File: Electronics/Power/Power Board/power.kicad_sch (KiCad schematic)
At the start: 58 parts, among them IC3 INA219AIDR, IC6 TPS54295PWPR, IC7 MP28167GQ-A-Z, J1 XT60PW-M, J3 XT60PW-F, SW1 SW_SPDT

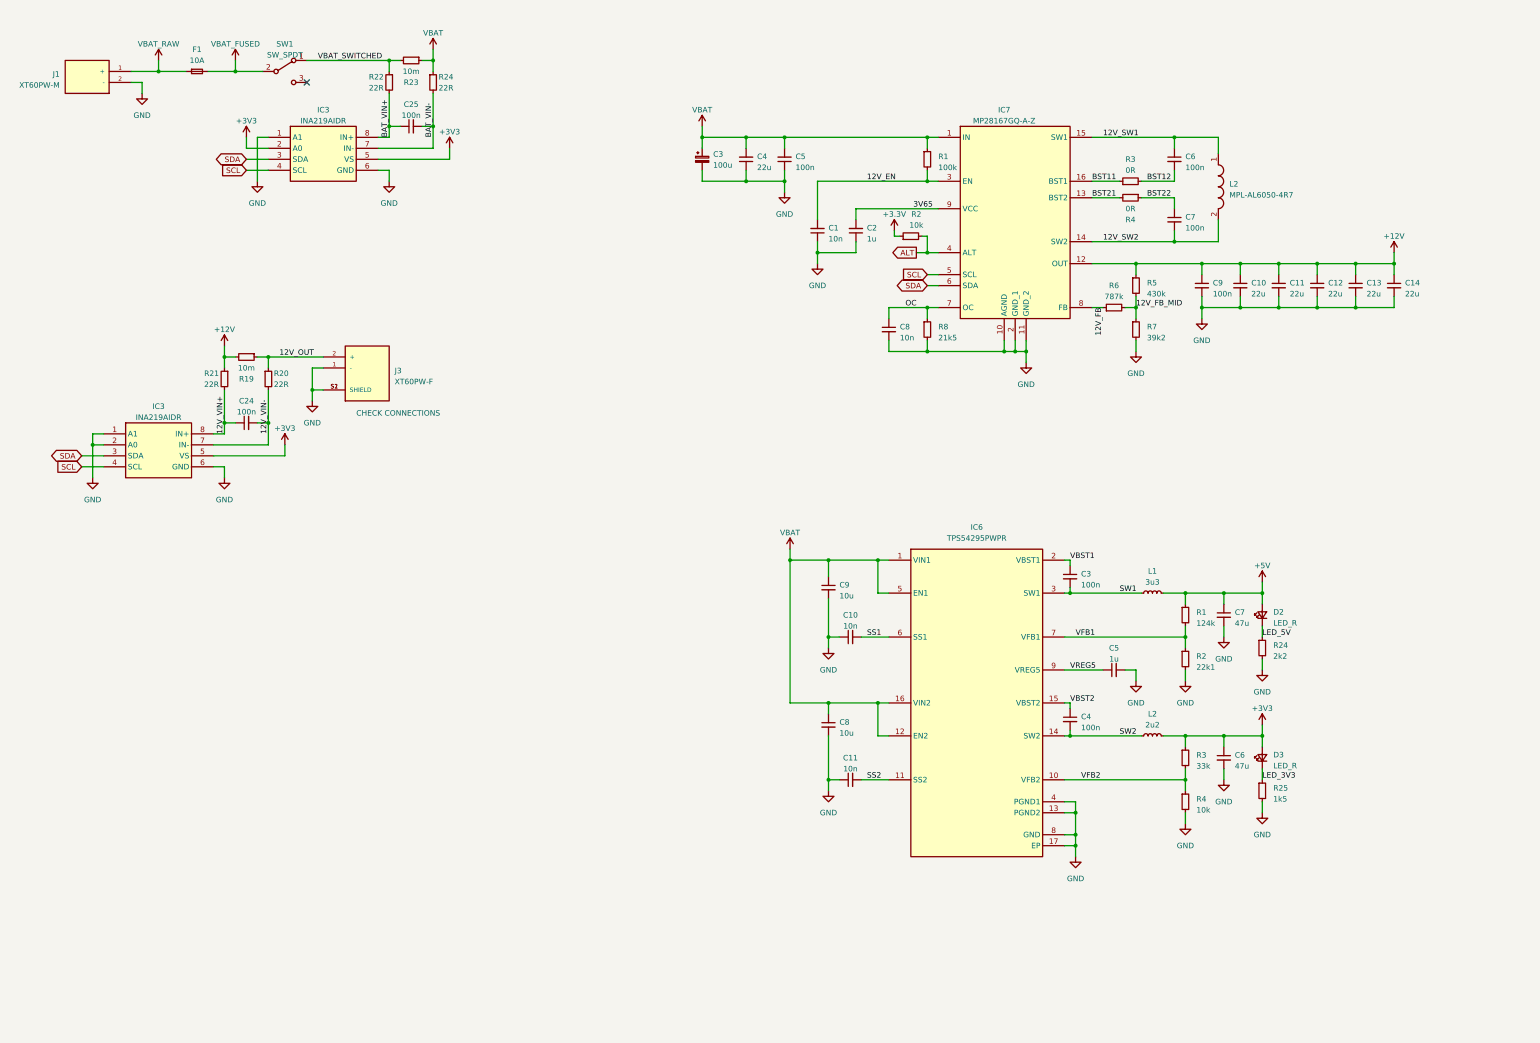
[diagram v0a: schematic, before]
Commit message: Motor driver + power board progress
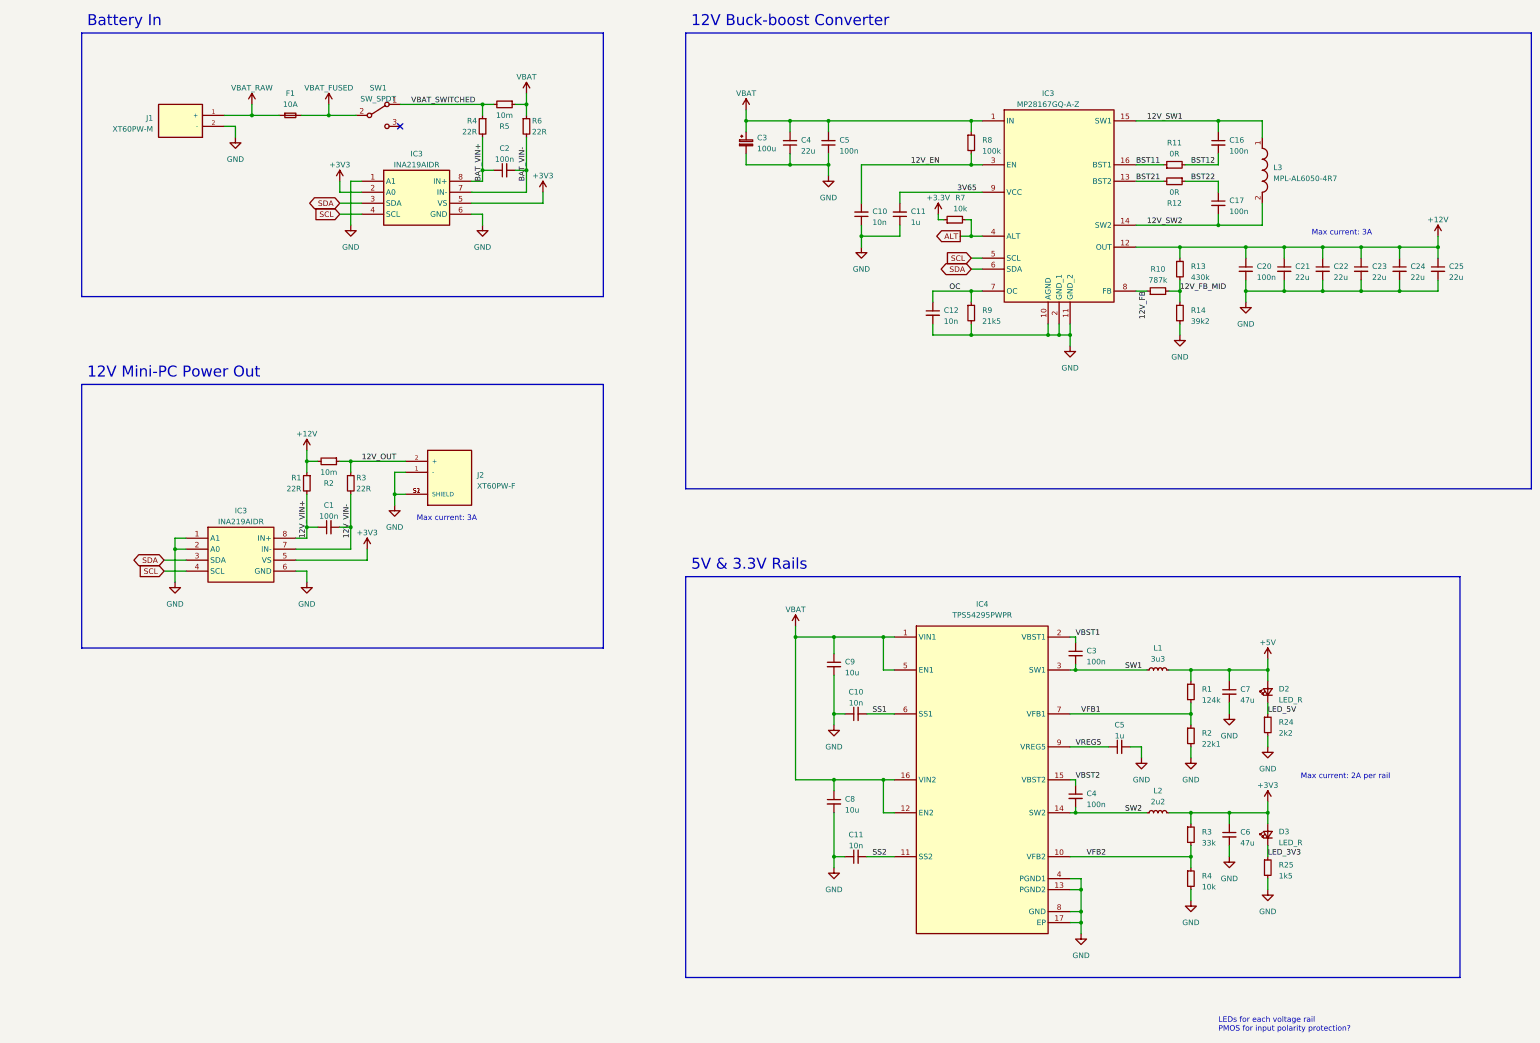
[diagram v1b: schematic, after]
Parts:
- SW1: footprint (none) -> MSL Footprints:Toggle_switch
- renumbered C24 to C1, C1 to C10, C2 to C11, C8 to C12, C6 to C16, C7 to C17, C25 to C2, C9 to C20, C10 to C21, C11 to C22, C12 to C23, C13 to C24, C14 to C25, IC7 to IC3, IC6 to IC4, J3 to J2, L2 to L3, R21 to R1, R6 to R10, R3 to R11, R4 to R12, R5 to R13, R7 to R14, R19 to R2, R20 to R3, R22 to R4, R23 to R5, R24 to R6, R2 to R7, R1 to R8, R8 to R9
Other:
- note added: "12V Buck-boost Converter"
- note added: "12V Mini-PC Power Out"
- note added: "5V & 3.3V Rails"
- note added: "Battery In"
- note added: "LEDs for each voltage rail PMOS for input polarity protection?"
- note added: "Max current: 2A per rail"
- note added: "Max current: 3A"
- note removed: "CHECK CONNECTIONS"
- moved on the sheet: C1, C10, C11, C12, C16, C17, C2, C20, C21, C22, C23, C24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

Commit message: PCB Schematic progress
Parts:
- removed C4: 22u, Capacitor_SMD:C_0402_1005Metric, symbol Device:C_Small
- added C42: 22u, Capacitor_SMD:C_0805_2012Metric, symbol Device:C_Small
- added J10, J11 (x2), J9: Conn_01x02_Pin, Connector_PinHeader_2.54mm:PinHeader_1x02_P2.54mm_Vertical, symbol Connector:Conn_01x02_Pin
- added J2 (x6): Screw_Terminal_01x02, TerminalBlock:TerminalBlock_bornier-2_P5.08mm, symbol Connector:Screw_Terminal_01x02
- C21, C22, C23, C24, C25: footprint Capacitor_SMD:C_0402_1005Metric -> Capacitor_SMD:C_0805_2012Metric
- C3: footprint (none) -> Capacitor_SMD:CP_Elec_6.3x7.7
- C8, C9: footprint Capacitor_SMD:C_0402_1005Metric -> Capacitor_SMD:C_0603_1608Metric
- D2, D3: value LED_R -> Green
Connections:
- net +5V: now also J10.1 (Pin_1), J11.1 (Pin_1), J11.1 (Pin_1), J9.1 (Pin_1)
- net GND: now also C42.2, J10.2 (Pin_2), J11.2 (Pin_2), J11.2 (Pin_2), J2.2 (Pin_2), J2.2 (Pin_2), J2.2 (Pin_2), J2.2 (Pin_2), J2.2 (Pin_2), J2.2 (Pin_2), J9.2 (Pin_2)
- net VBAT: now also C42.1, J2.1 (Pin_1), J2.1 (Pin_1), J2.1 (Pin_1), J2.1 (Pin_1), J2.1 (Pin_1), J2.1 (Pin_1)
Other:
- note added: "5V Fan Headers"
- note added: "VOUT Connectors"
- note removed: "LEDs for each voltage rail PMOS for input polarity protection?"
- moved on the sheet: C1, C10, C11, C12, C16, C17, C2, C20, C21, C3, C4, C5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

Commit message: PCB Schematics finished
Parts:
- renumbered C1 to C201, C2 to C202, C3 to C203, C42 to C204, C5 to C205, C10 to C210, C11 to C211, C12 to C212, C16 to C216, C17 to C217, C20 to C220, C21 to C221, C22 to C222, C23 to C223, C24 to C224, C25 to C225, IC3 to IC203, IC4 to IC204, J1 to J202, J2 to J209, L3 to L203, R1 to R201, R2 to R202, R3 to R203, R4 to R204, R5 to R205, R6 to R206, R7 to R207, R8 to R208, R9 to R209, R10 to R210, R11 to R211, R12 to R212, R13 to R213, R14 to R214, SW1 to SW201

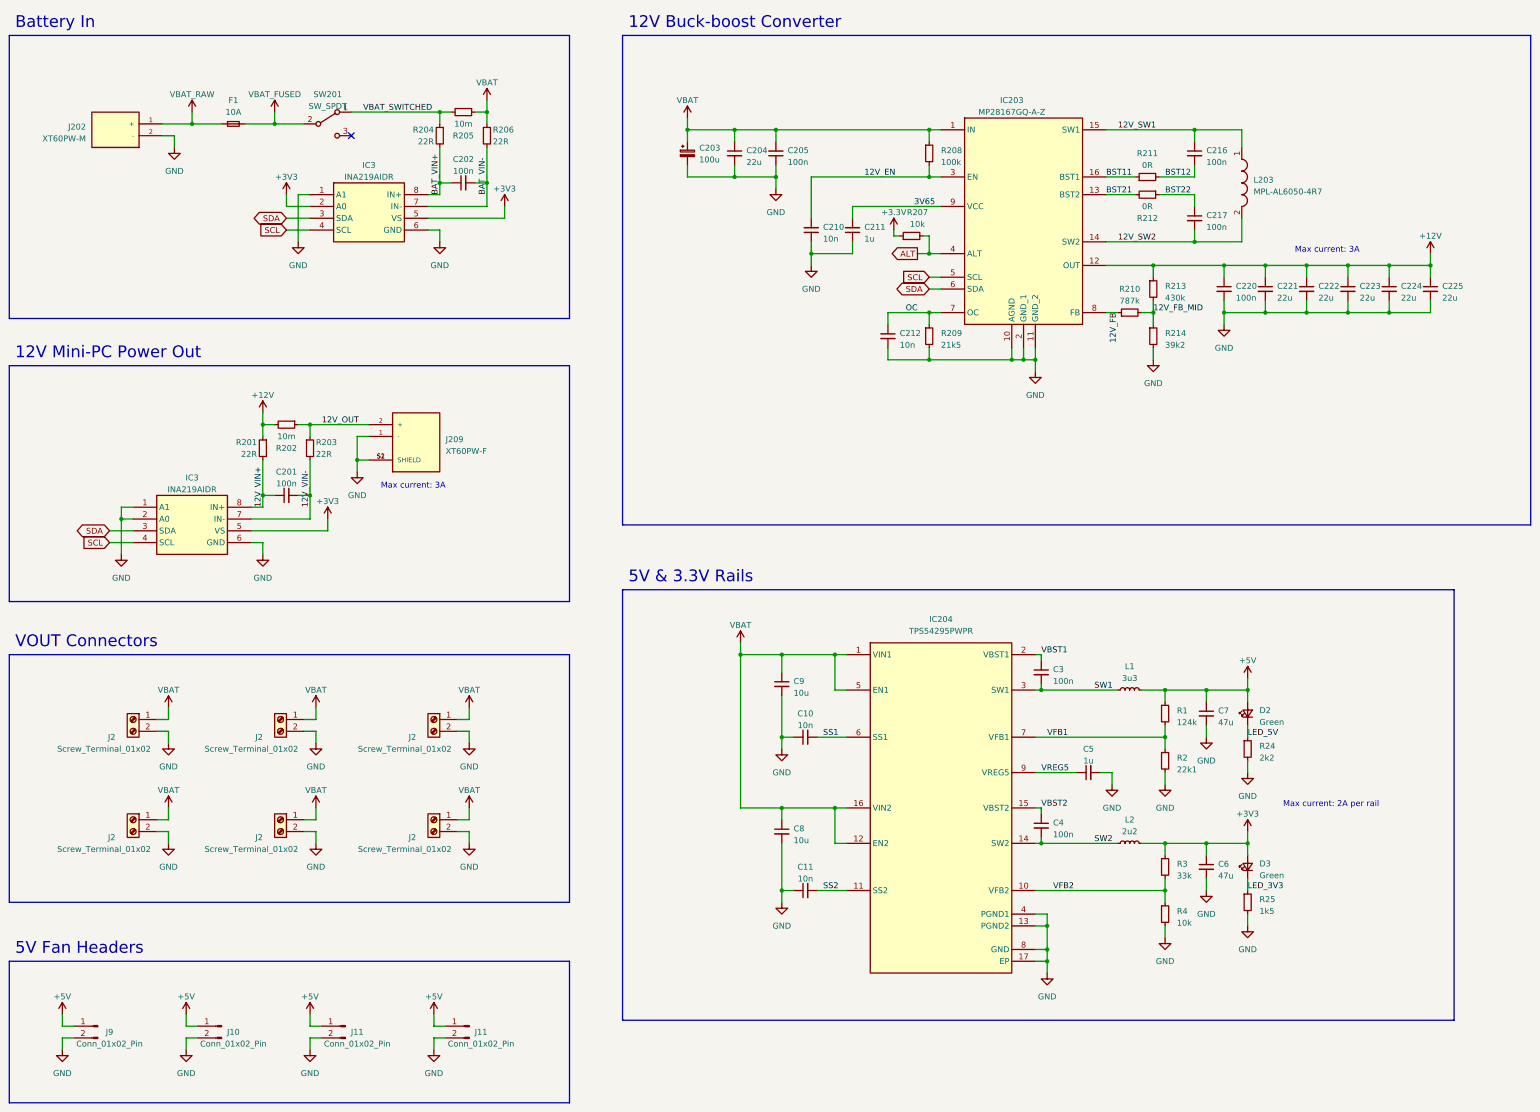
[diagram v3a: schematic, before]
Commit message: Schematic updates
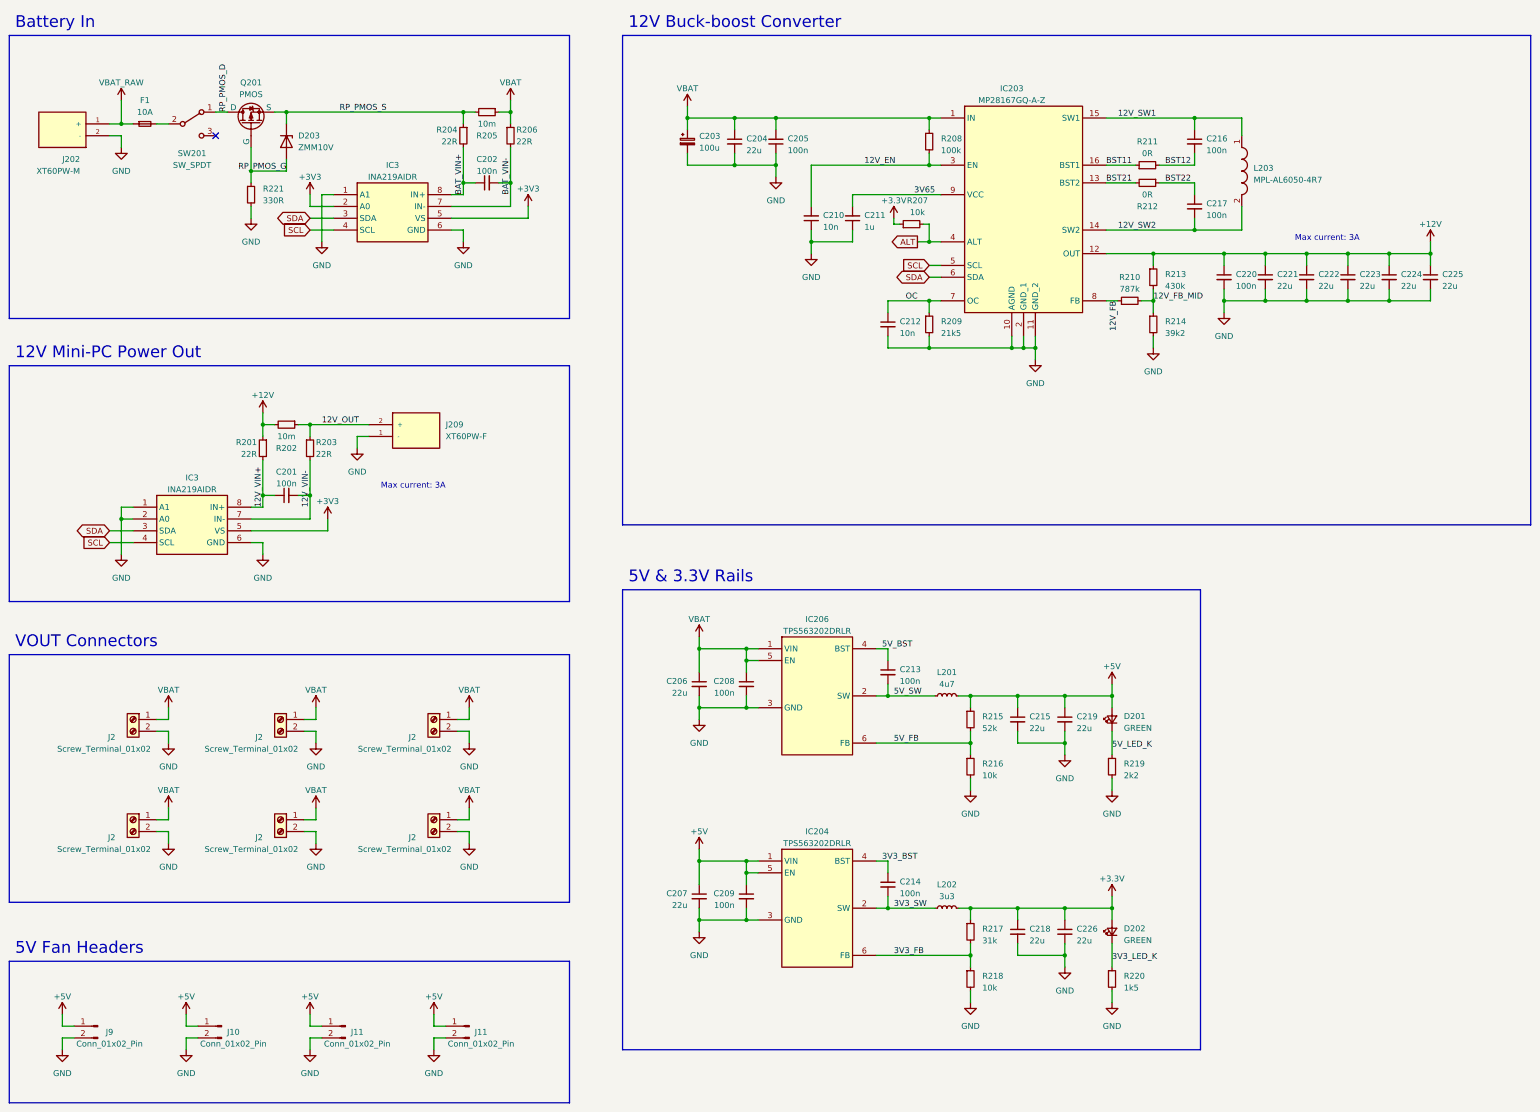
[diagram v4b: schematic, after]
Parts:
- removed C10, C11: 10n, Capacitor_SMD:C_0402_1005Metric, symbol Device:C_Small
- removed C3, C4: 100n, Capacitor_SMD:C_0402_1005Metric, symbol Device:C_Small
- removed C5: 1u, Capacitor_SMD:C_0402_1005Metric, symbol Device:C_Small
- removed C6, C7: 47u, Capacitor_SMD:C_0805_2012Metric, symbol Device:C_Small
- removed C8, C9: 10u, Capacitor_SMD:C_0603_1608Metric, symbol Device:C_Small
- removed D2, D3: Green, LED_SMD:LED_0603_1608Metric, symbol Device:LED_Small
- removed IC204: TPS54295PWPR, SOP65P640X120-17N, symbol TPS54295PWPR:TPS54295PWPR
- removed L1: 3u3, MSL Footprints:29332C, symbol Device:L_Small
- removed L2: 2u2, MSL Footprints:29222C, symbol Device:L_Small
- removed R1: 124k, Resistor_SMD:R_0402_1005Metric, symbol Device:R_Small
- removed R2: 22k1, Resistor_SMD:R_0402_1005Metric, symbol Device:R_Small
- removed R24: 2k2, Resistor_SMD:R_0402_1005Metric, symbol Device:R_Small
- removed R25: 1k5, Resistor_SMD:R_0402_1005Metric, symbol Device:R_Small
- removed R3: 33k, Resistor_SMD:R_0402_1005Metric, symbol Device:R_Small
- removed R4: 10k, Resistor_SMD:R_0402_1005Metric, symbol Device:R_Small
- added C206, C207, C215, C218, C219, C226: 22u, Capacitor_SMD:C_0603_1608Metric, symbol Device:C_Small
- added C208, C209, C213, C214: 100n, Capacitor_SMD:C_0402_1005Metric, symbol Device:C_Small
- added D201, D202: GREEN, LED_SMD:LED_0603_1608Metric, symbol Device:LED_Small
- added D203: ZMM10V, Diode_SMD:D_MiniMELF, symbol Diode:ZMMxx
- added IC204, IC206: TPS563202DRLR, MSL Footprints:SOTFL50P160X60-6N, symbol TPS563202DRLR:TPS563202DRLR
- added L201: 4u7, Inductor_SMD:L_Chilisin_BMRA00040420, symbol Device:L_Small
- added L202: 3u3, Inductor_SMD:L_Chilisin_BMRA00040420, symbol Device:L_Small
- added Q201: PMOS, symbol Simulation_SPICE:PMOS
- added R215: 52k, Resistor_SMD:R_0402_1005Metric, symbol Device:R_Small
- added R216, R218: 10k, Resistor_SMD:R_0402_1005Metric, symbol Device:R_Small
- added R217: 31k, Resistor_SMD:R_0402_1005Metric, symbol Device:R_Small
- added R219: 2k2, Resistor_SMD:R_0402_1005Metric, symbol Device:R_Small
- added R220: 1k5, Resistor_SMD:R_0402_1005Metric, symbol Device:R_Small
- added R221: 330R, Resistor_SMD:R_0402_1005Metric, symbol Device:R_Small
- IC203: footprint MSL Footprints:MP28167GQAZ -> MP28167GQAZ
- J202: footprint MSL Footprints:AMASS_XT60PW-M -> Connector_AMASS:AMASS_XT60PW-M_1x02_P7.20mm_Horizontal
- J209: footprint AMASS_XT60PW-F -> Connector_AMASS:AMASS_XT60PW-F_1x02_P7.20mm_Horizontal
- L203: footprint MSL Footprints:MPLAL60504R7 -> MPLAL60504R7
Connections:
- net +3.3V: now also C218.1, C226.1, D202.2 (A), L202.2, R217.1
- net +5V: now also C207.1, C209.1, C215.1, C219.1, D201.2 (A), IC204.1 (VIN), IC204.5 (EN), L201.2, R215.1
- net GND: now also C206.2, C207.2, C208.2, C209.2, C215.2, C218.2, C219.2, C226.2, IC204.3 (GND), IC206.3 (GND), R216.2, R218.2, R219.2, R220.2, R221.2; no longer J209.S1 (SHIELD), J209.S2 (SHIELD)
- net VBAT: now also C206.1, C208.1, IC206.1 (VIN), IC206.5 (EN)
- net VBAT_FUSED: no longer names the net of F1.2, SW201.2 (B)
- net VBAT_SWITCHED renamed RP_PMOS_S
- net RP_PMOS_S: now also D203.1 (K), Q201.3 (S); no longer SW201.1 (A)
- new net 3V3_BST: C214.1, IC204.4 (BST)
- new net 3V3_FB: IC204.6 (FB), R217.2, R218.1
- new net 3V3_LED_K: D202.1 (K), R220.1
- new net 3V3_SW: C214.2, IC204.2 (SW), L202.1
- new net 5V_BST: C213.1, IC206.4 (BST)
- new net 5V_FB: IC206.6 (FB), R215.2, R216.1
- new net 5V_LED_K: D201.1 (K), R219.1
- new net 5V_SW: C213.2, IC206.2 (SW), L201.1
- new net RP_PMOS_D: Q201.1 (D), SW201.1 (A)
- new net RP_PMOS_G: D203.2 (A), Q201.2 (G), R221.1
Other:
- note removed: "Max current: 2A per rail"
- moved on the sheet: C202, C203, C204, C205, C210, C211, C212, C216, C217, C220, C221, C222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
